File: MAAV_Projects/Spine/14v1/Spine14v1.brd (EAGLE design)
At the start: 119.4 x 101.6 mm, 84 parts, among them J7 MA04-1, Q1 MOSFET-NCHANNELBSS138, Q2 MOSFET-NCHANNELSMD, Q21 P-MOSFET-SO8POWER-PAK, Q22 P-MOSFET-SO8POWER-PAK, Q23 P-MOSFET-SO8POWER-PAK, Q24 P-MOSFET-SO8POWER-PAK, Q3 MOSFET-NCHANNELSMD, Q4 MOSFET-NCHANNELSMD, Q6 16MHz, Q7 CRYSTAL_16MHZ_SMD, U1 ATMEGA328-AU, U2 REG_3V_8SOIC

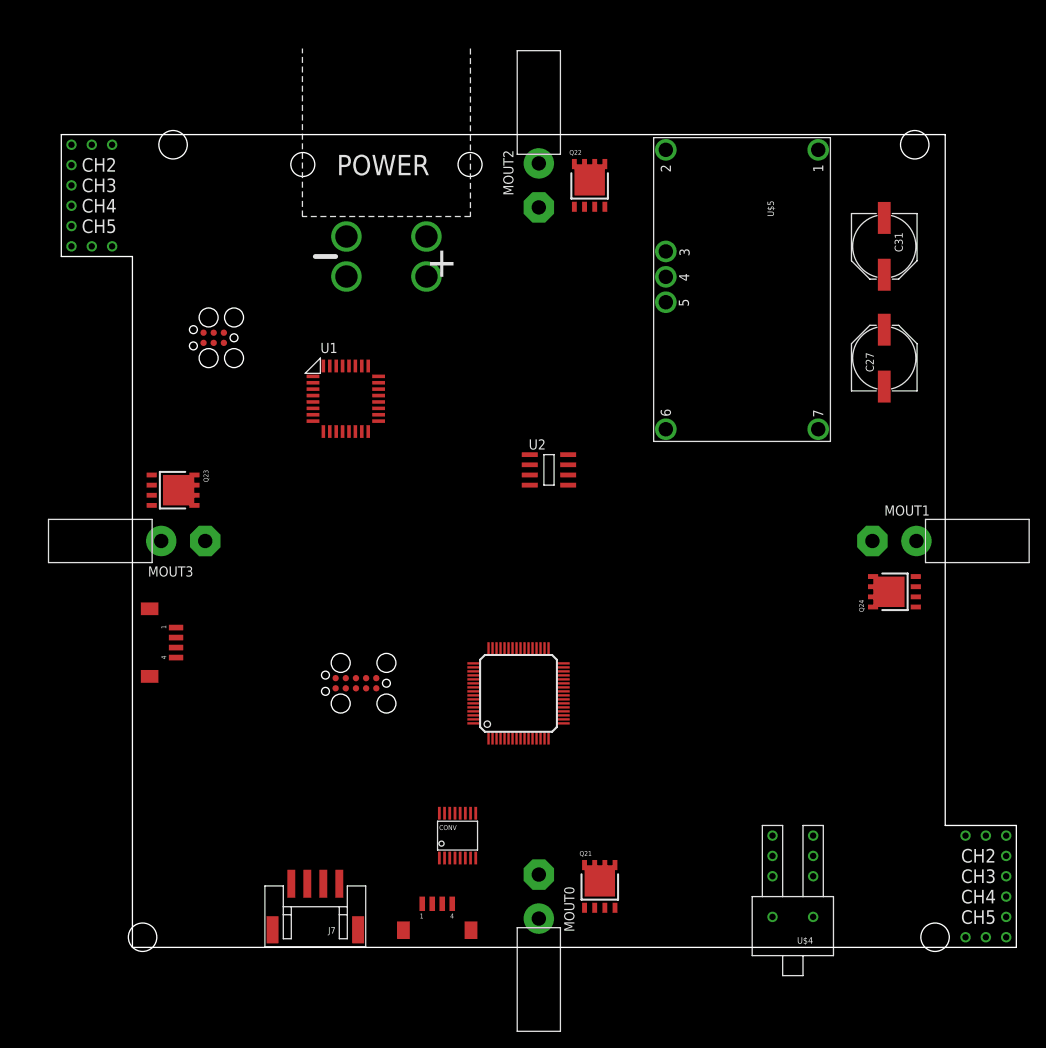
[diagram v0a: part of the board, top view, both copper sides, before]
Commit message: updated dims and holes.  added roundovers to hard corners of baord. added a drawing of the body that the board mounts to.
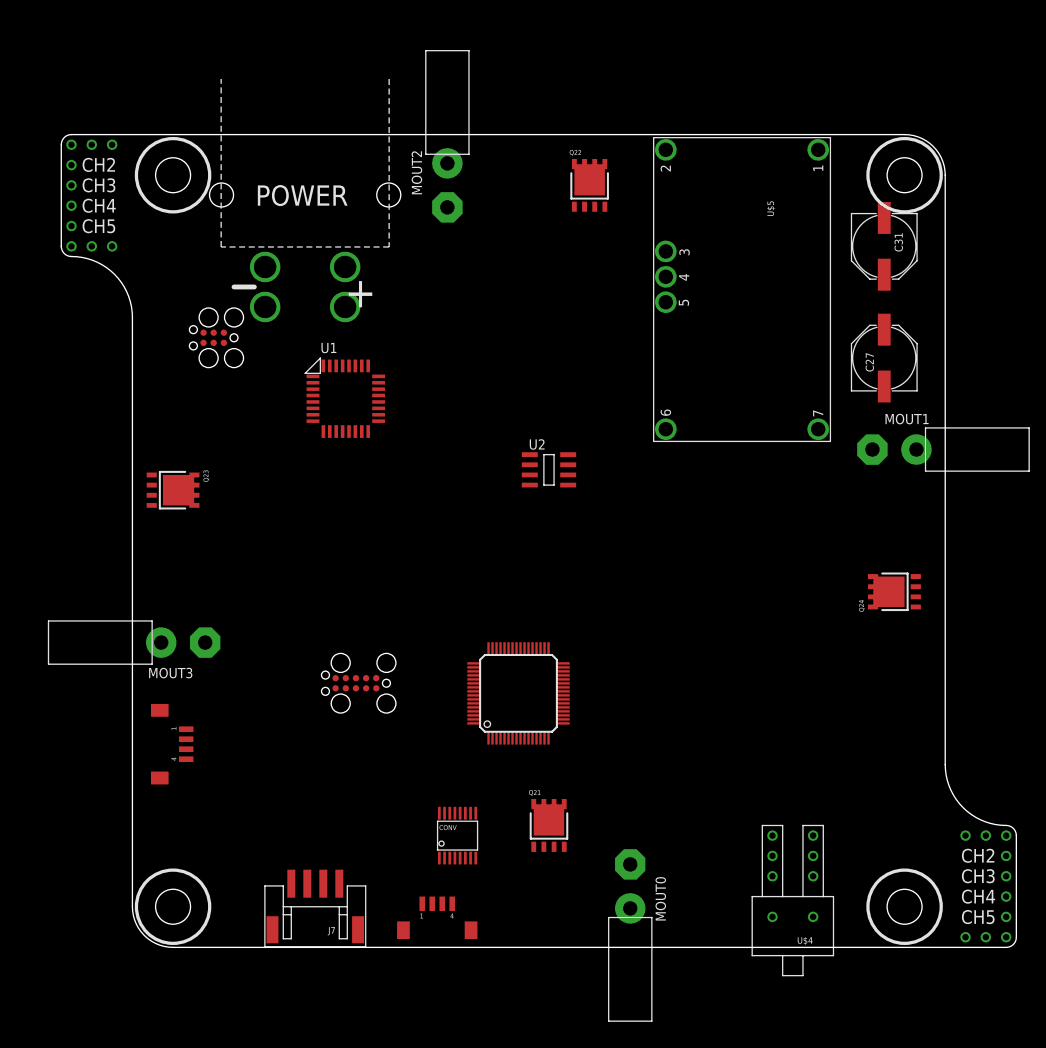
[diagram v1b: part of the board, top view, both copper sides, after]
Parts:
- moved I2C_1 12.8 mm to (7.62, 25.4)
- moved MOUT3 12.7 mm to (6.35, 38.1)
- moved MOUT0 11.5 mm to (62.2, 7.62)
- moved MOUT1 11.4 mm to (95.2, 62.2)
- moved MOUT2 11.4 mm to (39.4, 95.2)
- moved V_BATT1 10.9 mm to (21.6, 82.5)
- moved Q21 9.92 mm to (52.1, 15.2)
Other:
- outline, holes or cut-outs redrawn
- board text removed: "Confirm dimentions of board get locations and size of holes"

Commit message: started routing
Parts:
- removed C11: 4.7uF, rcl:C0805
- removed LED2, LED3, LED4: GREEN, Jon_LIB:CHIPLED_0603
- removed LED5: red, Jon_LIB:CHIPLED_0603
- removed LED6: green, Jon_LIB:CHIPLED_0603
- removed LED7: blue, Jon_LIB:CHIPLED_0603
- removed R44, R47, R48: 750, Jon_LIB:R0805
- removed S1: SWITCH-OFF-MOM_SMD_TACTILE, MAAV:SWITCH_TACT_NO_SPST_PAN
- removed U2: REG_3V_8SOIC, MAAV:8-SOIC
- added ATOM_POW, DJI_POW: POWER_CONN_VERT, MAAV:POWER_CONN
- added C15: 1.0uF, Jon_LIB:C0805
- added C16: 2.2uF, Jon_LIB:C0805
- added D1, D2: LED_RGB_CA, Jon_LIB:LED_RGB_0606
- added Q5: P-MOSFET-SO8POWER-PAK, Jon_LIB:SO-8_POWER-PAK
- added Q8: MOSFET-NCHANNELSMD, Jon_LIB:SOT23-3
- added R10: 200, Jon_LIB:R0603
- added R14: 100, Jon_LIB:R0603
- added R7, R8: 2.2k, Jon_LIB:R0603
- added S2: (no value), Jon_LIB:TACT-MOM-SMD
- added U$1, U$6: CRYSTAL_403C11E16, imu:4-SMD-SWITCH
- added U3: XC6210, MAAV:SOT-25
- C10: value 0.1uF -> 10nF; device rcl:C0603 -> Jon_LIB:C0603
- C13, C14: device Jon_LIB:C0603 -> Jon_LIB:C0805
- C19, C20: value 22pF -> 10pF
- C4: device rcl:C0603 -> Jon_LIB:C0603
- LED1: device MAAV_13v1:JON_LIB_CHIPLED_0603 -> Jon_LIB:CHIPLED_0603
- MOUT0, MOUT1, MOUT2, MOUT3: value POWER_CONN -> POWER_CONN_VERT
- Q1: value MOSFET-NCHANNELBSS138 -> MOSFET-NCHANNELSMD; device SparkFun-DiscreteSemi:SOT23 -> Jon_LIB:SOT23-3
- Q6: value 16MHz -> MOSFET-NCHANNELSMD; device crystal:HC49UP -> Jon_LIB:SOT23-3
- Q7: value CRYSTAL_16MHZ_SMD -> MOSFET-NCHANNELSMD; device Jon_LIB:4-SMD_DFN -> Jon_LIB:SOT23-3
- R1, R11, R12, R15, R2, R3, R9: device rcl:R0603 -> Jon_LIB:R0603
- R13: value 250k -> 100; device rcl:R0603 -> Jon_LIB:R0603
- R16: value 330 -> 100; device rcl:R0603 -> Jon_LIB:R0603
- moved C14 264.8 mm to (64.5, 21.1), turned to 270 degrees
- moved C38 260.3 mm to (54.1, 20.3), turned to 90 degrees
- moved C40 260.0 mm to (43.9, 20.8), turned to 270 degrees
- moved C37 255.4 mm to (53.8, 14.2), turned to 90 degrees
- moved C39 253.2 mm to (39.6, 17.8), turned to 270 degrees
- moved C10 252.5 mm to (72.3, 26.2)
- moved C13 249.2 mm to (62.5, 41.7), turned to 90 degrees
- moved LED1 249.1 mm to (56.9, 73.9), turned to 180 degrees
- moved C41 247.1 mm to (35.6, 15.0), turned to 90 degrees
- moved C12 245.6 mm to (65.3, 42.4)
- moved R12 236.1 mm to (91.4, 22.4)
- moved R15 236.1 mm to (86.4, 22.4)
- moved C5 235.8 mm to (70.1, 20.8), turned to 270 degrees
- moved R6 233.6 mm to (74.9, 4.32), turned to 270 degrees
- moved R5 232.7 mm to (73.4, 4.32), turned to 270 degrees
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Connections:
- removed net N$33: LED3.A, R47.1
- removed net N$34: LED4.A, R48.1
- removed net N$9: LED2.A, R44.1
- new net N$21: DJI_POW.P1, Q5.D1, Q5.D2, Q5.D3, Q5.D4, Q5.D5
- new net N$22: Q6.3, R14.1
- new net N$23: D2.2, R10.2
- new net N$24: D2.3, R13.2
- new net N$25: D2.4, R14.2
- net +3V3: now also C16.1, U3.5; no longer C11.1, R13.2, U2.P$7, U2.P$8
- net +5V: now also ATOM_POW.P1, C15.2, D1.1, D2.1, U3.1, U3.3; no longer C10.1, LED5.A, LED6.A, LED7.A, U2.P$5, U2.P$6
- net 5V_ENABLE: now also U$4.P$5; no longer U$4.P$2
- net A_XTAL1: now also U$6.3; no longer Q7.X1
- net A_XTAL2: now also U$6.1; no longer Q7.X2
- net GND: now also ATOM_POW.P2, C15.1, C16.2, DJI_POW.P2, Q6.2, Q7.2, Q8.2, R7.1, R8.1, S2.S, S2.S1, U$1.2, U$1.4, U$4.P$6, U$6.2, U$6.4, U3.2; no longer C11.2, LED2.C, LED3.C, LED4.C, S1.2, S1.4, U$4.P$1, U2.P$3, U2.P$4
- net KILL_5: now also U1.P$24
- net LED1: now also Q8.1; no longer R48.2
- net LED2: now also Q7.1; no longer R47.2
- net LED3: now also Q6.1; no longer R44.2
- net M_ENABLE: now also Q5.G, U$4.P$2; no longer U$4.P$5
- net M_EN_PRE: now also U$4.P$1; no longer U$4.P$6
- net N$10: now also R11.1, S2.P, S2.P1; no longer R13.1, U2.P$2
- net N$12: now also Q8.3, R10.1; no longer R11.1, S1.1, S1.3
- net N$19: now also D1.4; no longer LED7.C
- net N$20: now also Q7.3, R13.1; no longer C26.1, C3.1, C31.+, U$5.2
- net N$6: now also D1.2; no longer LED5.C
- net N$7: now also D1.3; no longer LED6.C
- net RESET: now also C10.1
- net SCL_3V3: now also R8.2
- net SDA_3V3: now also R7.2
- net T_OSC0: now also U$1.3; no longer Q6.2
- net T_OSC1: now also U$1.1; no longer Q6.1
- net V_BATT: now also C26.1, C3.1, C31.+, Q5.S1, Q5.S2, Q5.S3, U$5.2
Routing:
- net +5V: track 0.00 -> 348.2 mm, vias 0 -> 3
- net RC_1: track 0.00 -> 69.0 mm
- net RC_2: track 0.00 -> 66.0 mm
- net RC_3: track 0.00 -> 61.8 mm
- net RC_4: track 0.00 -> 59.9 mm
- net RC_6: track 0.00 -> 59.5 mm
- net RC_5: track 0.00 -> 59.5 mm
- net SDA_3V3: track 0.00 -> 56.0 mm, vias 0 -> 2
- net SCL_3V3: track 0.00 -> 53.4 mm, vias 0 -> 2
- net KILL_1: track 0.00 -> 32.8 mm
- net GND: track 0.00 -> 32.3 mm, vias 0 -> 35
- net KILL_2: track 0.00 -> 29.7 mm
- net +3V3: track 0.00 -> 28.9 mm, vias 0 -> 1
- net KILL_6: track 0.00 -> 28.8 mm
- net KILL_SIG: track 0.00 -> 28.1 mm
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- added copper zone on layer 1, net +5V
- added copper zone on layer 1, net GND
- added copper zone on layer 15, net GND
- added copper zone on layer 2, net GND
- added copper zone on layer 1, net N$15
- added copper zone on layer 1, net N$16
- added copper zone on layer 1, net N$17
- added copper zone on layer 1, net N$2
- added copper zone on layer 1, net N$21
- added copper zone on layer 1, net V_BATT
- added copper zone on layer 15, net V_BATT
- added copper zone on layer 16, net V_BATT
- added copper zone on layer 2, net V_BATT
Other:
- board size 119.4 x 101.6 mm -> 124.5 x 101.6 mm
- board text added: "Kill Switch"
- board text added: "RC Control"

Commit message: Routed most of the ATMega. Can there be traces in the Route2 layer?
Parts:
- moved Q1 8.68 mm to (16.3, 34.3)
- moved C24 6.48 mm to (17.5, 67.8), turned to 180 degrees
- moved C40 6.25 mm to (50.0, 19.4), turned to 180 degrees
- moved C23 5.84 mm to (17.5, 66.0), turned to 180 degrees
- moved C21 4.88 mm to (17.5, 62.5), turned to 180 degrees
- moved CONV 2.82 mm to (50.0, 15.1)
- moved C38 2.80 mm to (55.9, 18.2)
- moved C4 2.37 mm to (29.2, 56.5), turned to 0 degrees
- moved C22 2.17 mm to (17.5, 64.3), turned to 180 degrees
- moved C37 1.91 mm to (55.8, 14.4)
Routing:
- net GND: track 32.3 -> 151.8 mm, vias 35 -> 58
- net RESET: track 10.7 -> 46.3 mm
- net LED3: track 0.00 -> 26.0 mm, vias 0 -> 2
- net SCL_3V3: track 53.4 -> 77.9 mm, vias 2 -> 4
- net KILL_5: track 25.0 -> 49.3 mm, vias 0 -> 2
- net SDA_3V3: track 56.0 -> 79.9 mm, vias 2 -> 4
- net LED2: track 0.00 -> 19.9 mm
- net +3V3: track 28.9 -> 41.5 mm
- net +5V: track 348.2 -> 353.6 mm
- net N$36: track 0.00 -> 5.34 mm
- net A_AREF: track 0.00 -> 4.83 mm
- net N$14: track 0.00 -> 4.47 mm
- net N$35: track 0.00 -> 3.78 mm
- net N$32: track 0.00 -> 3.14 mm
- net KILL_4: track 26.3 -> 29.4 mm
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- added copper zone on layer 1, net +3V3
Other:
- board text added: "JSON IS SOOOO COOOOL"

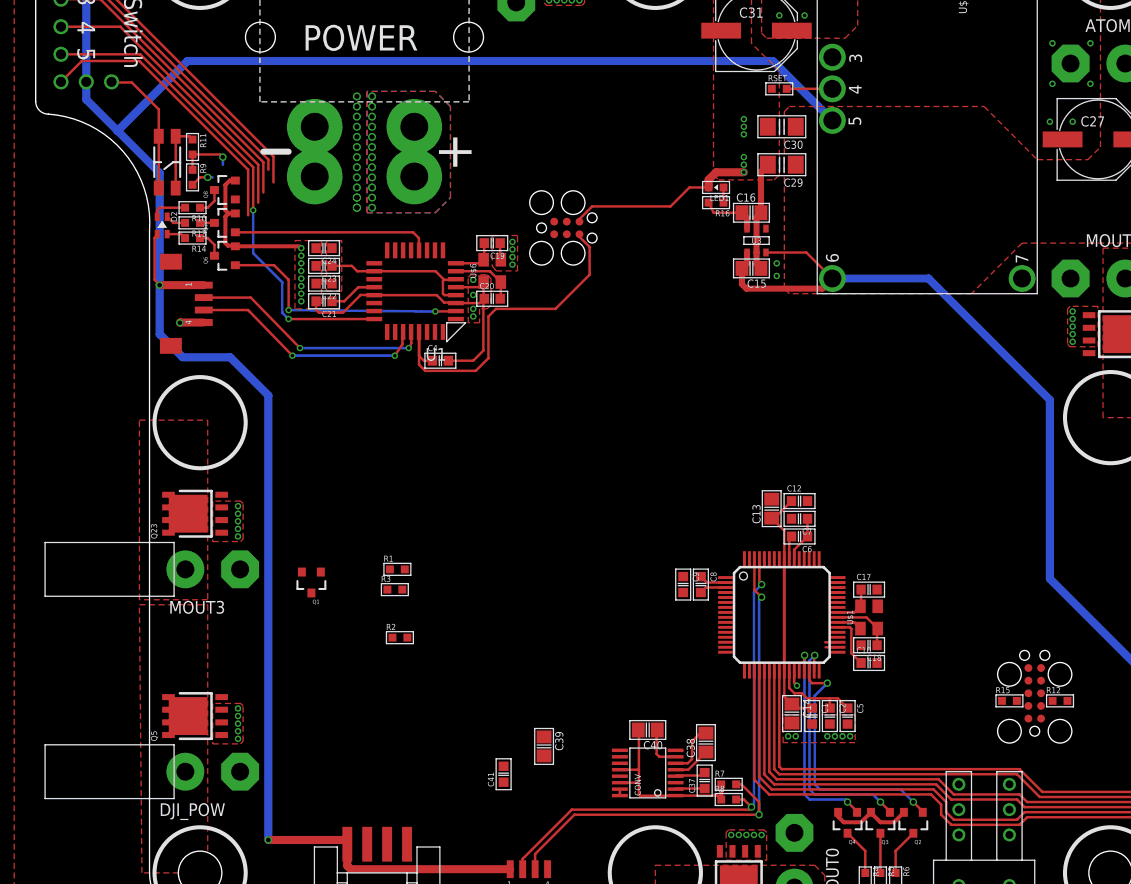
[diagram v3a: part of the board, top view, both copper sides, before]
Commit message: removed a few traces cuz i didn't realize Top layer was a huge GND polygon. although i fail to see the difference between the Top GND polygon and the Route2 GND polygon
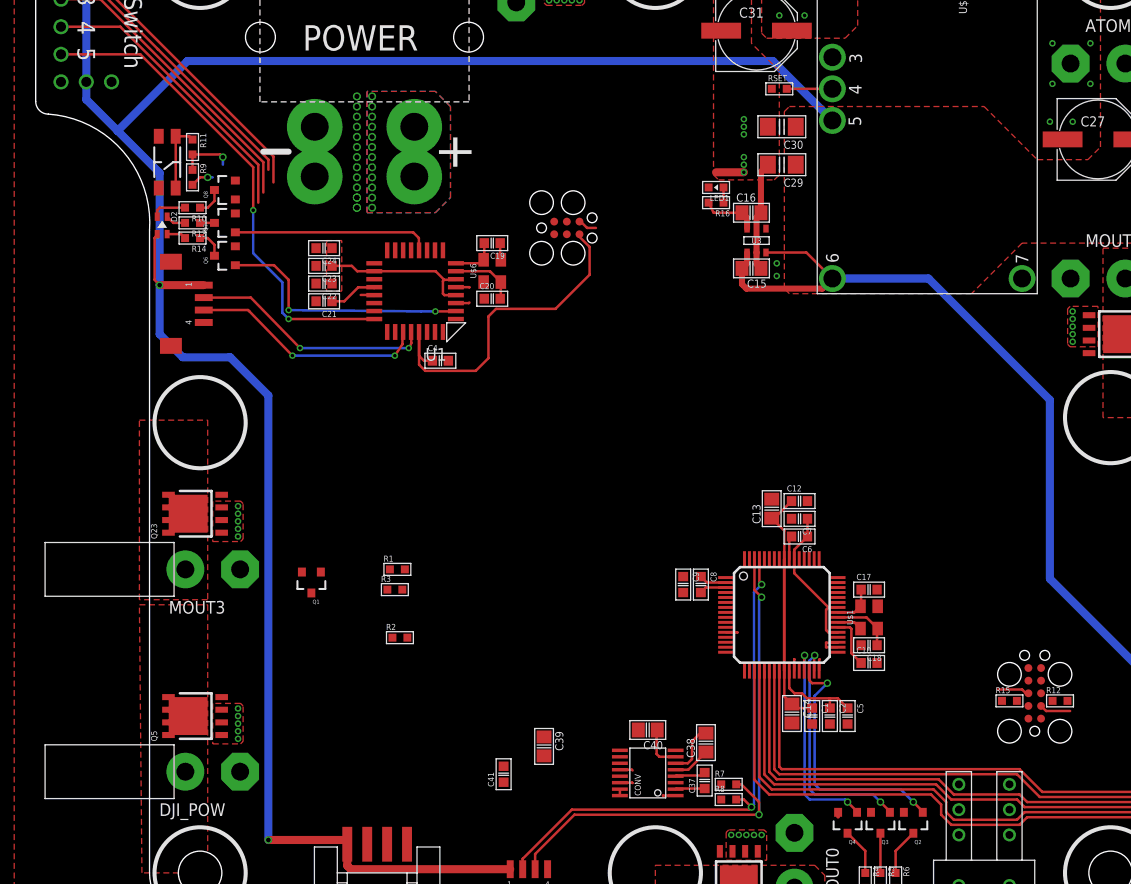
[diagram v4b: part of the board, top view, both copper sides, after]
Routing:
- net GND: track 151.8 -> 47.4 mm, vias 58 -> 34
- net KILL_6: track 28.8 -> 0.00 mm
- net +3V3: track 41.5 -> 52.3 mm

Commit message: routed some more (almost finished). Added some micro swtiches to Jon_LIB
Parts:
- added S1: SWITCH_DPDT_VERT_TOGGLE, Jon_LIB:NKK_VERT_SWITCH_6PIN
- added S3, S4: SWITCH_SPDT_ILUMINATED_2COLOR_VERT_ILLUMINATED, Jon_LIB:NKK_VERT_SWITCH_6PIN
- moved Q1 80.6 mm to (94.5, 15.0), turned to 90 degrees
- moved R3 74.7 mm to (97.0, 15.0), turned to 270 degrees
- moved R1 71.2 mm to (91.2, 9.65)
- moved R2 68.2 mm to (91.9, 15.0), turned to 270 degrees
- moved C41 24.4 mm to (59.1, 21.3), turned to 270 degrees
- moved C39 22.6 mm to (61.9, 21.6), turned to 180 degrees
- moved C40 19.4 mm to (66.3, 30.1), turned to 0 degrees
- moved CONV 16.0 mm to (61.9, 25.8)
- moved C37 14.6 mm to (67.2, 23.5)
- moved C38 14.3 mm to (67.1, 27.1)
- moved C1 13.1 mm to (74.2, 31.5)
- moved C2 13.1 mm to (75.9, 31.5)
- moved C5 13.1 mm to (77.7, 31.5)
- moved U$3 13.1 mm to (71.1, 41.7)
- moved C13 13.1 mm to (70.1, 52.3)
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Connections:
- net KILL_4: now also U$3.P$7; no longer U$3.P$8
- net KILL_5: now also U$3.P$8; no longer U$3.P$7
- net KILL_6: now also U$3.P$9; no longer U$3.P$6
- net KILL_SIG: now also U$3.P$6; no longer U$3.P$9
- net LED1: now also U1.P$12; no longer U1.P$13
- net LED2: now also U1.P$13; no longer U1.P$12
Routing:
- net M_ENABLE: track 0.00 -> 262.8 mm, vias 0 -> 6
- net +3V3: track 52.3 -> 198.7 mm, vias 1 -> 10
- net 5V_ENABLE: track 0.00 -> 115.4 mm
- net MOTOR_LOGIC: track 0.00 -> 114.9 mm, vias 0 -> 2
- net KILL_6: track 0.00 -> 108.5 mm, vias 0 -> 2
- net RESET: track 46.3 -> 143.9 mm
- net KILL_SIG: track 30.1 -> 122.9 mm, vias 0 -> 3
- net SCL_3V3: track 77.9 -> 161.6 mm
- net KILL_2: track 29.7 -> 110.3 mm, vias 0 -> 2
- net KILL_4: track 29.4 -> 109.3 mm, vias 0 -> 2
- net KILL_1: track 32.8 -> 112.6 mm, vias 0 -> 2
- net SDA_3V3: track 79.9 -> 159.1 mm
- net KILL_5: track 49.3 -> 120.4 mm, vias 2 -> 3
- net RS-232_RX1: track 0.00 -> 50.6 mm, vias 0 -> 2
- net RS-232_TX1: track 0.00 -> 46.4 mm, vias 0 -> 2
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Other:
- board text removed: "JSON IS SOOOO COOOOL"
